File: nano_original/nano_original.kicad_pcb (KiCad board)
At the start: 2 copper layers, 43.2 x 18 mm, 29 parts, among them J1 USB_B_Micro, J2 Conn_01x15, J3 Conn_01x15, J4 Conn_02x03_Odd_Even, SW1 SW_Push, U1 LM1117MP-5.0, U2 FT231XS, U3 ATmega328P-MUR, Y1 16MHz

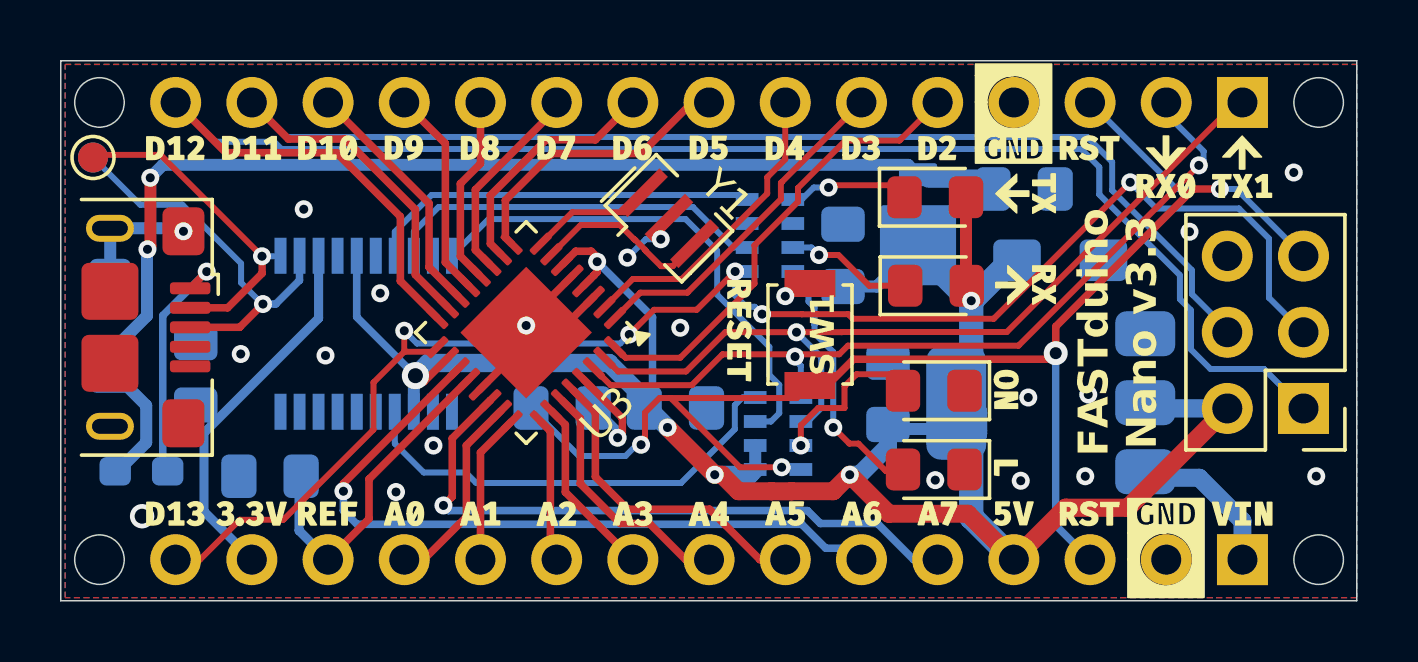
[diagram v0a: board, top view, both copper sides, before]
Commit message: critical fix: swap tx and rx between atmega328p and ft231 (smooth brain moment)
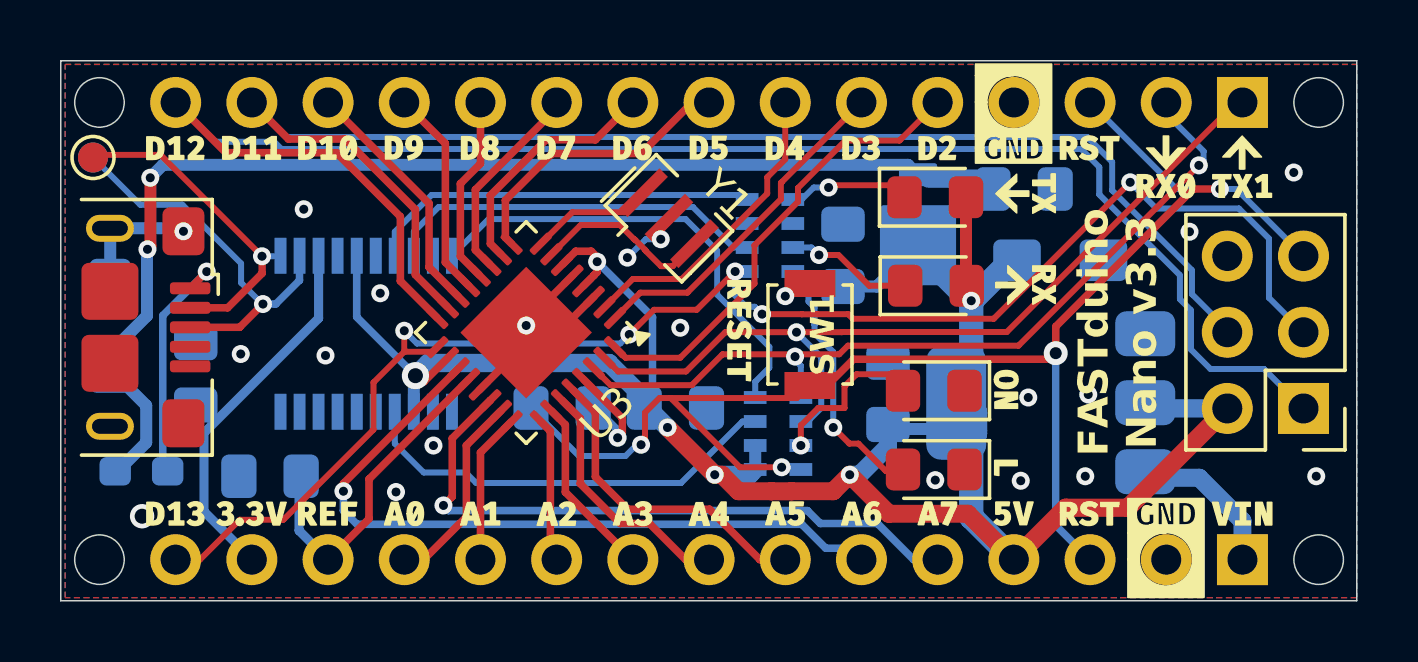
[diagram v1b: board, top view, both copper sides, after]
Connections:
- U2 pad 20: /TX -> /RX
- U2 pad 4: /RX -> /TX
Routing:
- net /TX: track 17.0 -> 14.5 mm
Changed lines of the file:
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@@
 			(size 1.2 0.4)
 			(layers "B.Cu" "B.Mask" "B.Paste")
-			(net 3 "/RX")
+			(net 6 "/TX")
 			(pinfunction "RXD")
 			(pintype "input")
@@
 			(size 1.2 0.4)
 			(layers "B.Cu" "B.Mask" "B.Paste")
-			(net 6 "/TX")
+			(net 3 "/RX")
 			(pinfunction "TXD")
 			(pintype "output")
@@
 	)
 	(segment
-		(start 79.825 88.075)
-		(end 73 88.075)
+		(start 81.02918 81.79628)
+		(end 81.02918 80.32918)
 		(width 0.2)
 		(layer "B.Cu")
@@
 	)
 	(segment
-		(start 72.65 87.725)
-		(end 71.25 87.725)
+		(start 82.770254 84.229746)
+		(end 82.770254 83.537354)
 		(width 0.2)
 		(layer "B.Cu")
@@
 	)
 	(segment
-		(start 81.619 86.281)
-		(end 79.825 88.075)
+		(start 73.413 79.277)
+		(end 72.19 80.5)
 		(width 0.2)
 		(layer "B.Cu")
@@
 	)
 	(segment
-		(start 81.619 85.481)
-		(end 81.619 86.281)
+		(start 82.3 84.7)
+		(end 82.770254 84.229746)
 		(width 0.2)
 		(layer "B.Cu")
@@
 	)
 	(segment
-		(start 81.875 85.225)
-		(end 81.619 85.481)
+		(start 79.977 79.277)
+		(end 73.413 79.277)
 		(width 0.2)
 		(layer "B.Cu")
@@
 	)
 	(segment
-		(start 73 88.075)
-		(end 72.65 87.725)
+		(start 82.770254 83.537354)
+		(end 81.02918 81.79628)
 		(width 0.2)
 		(layer "B.Cu")
@@
 	)
 	(segment
-		(start 70.285 86.76)
-		(end 70.285 85.7)
+		(start 82.3 85.225)
+		(end 82.3 84.7)
 		(width 0.2)
 		(layer "B.Cu")
@@
 	)
 	(segment
-		(start 82.3 85.225)
-		(end 81.875 85.225)
-		(width 0.2)
-		(layer "B.Cu")
-		(net 3)
-	)
-	(segment
-		(start 71.25 87.725)
-		(end 70.285 86.76)
+		(start 81.02918 80.32918)
+		(end 79.977 79.277)
 		(width 0.2)
 		(layer "B.Cu")
@@
 	)
 	(segment
-		(start 81.02918 80.32918)
-		(end 79.977 79.277)
+		(start 70.285 86.76)
+		(end 70.285 85.7)
 		(width 0.2)
 		(layer "B.Cu")
@@
 	)
 	(segment
-		(start 81.02918 81.79628)
-		(end 81.02918 80.32918)
+		(start 71.25 87.725)
+		(end 70.285 86.76)
 		(width 0.2)
 		(layer "B.Cu")
@@
 	)
 	(segment
-		(start 82.770254 84.470254)
-		(end 82.770254 83.537354)
+		(start 81.875 86.025)
+		(end 79.825 88.075)
 		(width 0.2)
 		(layer "B.Cu")
@@
 	)
 	(segment
-		(start 82.825 86.025)
-		(end 83.1 85.75)
+		(start 82.3 86.025)
+		(end 81.875 86.025)
 		(width 0.2)
 		(layer "B.Cu")
@@
 	)
 	(segment
-		(start 79.977 79.277)
-		(end 73.413 79.277)
+		(start 79.825 88.075)
+		(end 73 88.075)
 		(width 0.2)
 		(layer "B.Cu")
@@
 	)
 	(segment
-		(start 83.1 85.75)
-		(end 83.1 84.8)
+		(start 73 88.075)
+		(end 72.65 87.725)
 		(width 0.2)
 		(layer "B.Cu")
@@
 	)
 	(segment
-		(start 82.770254 83.537354)
-		(end 81.02918 81.79628)
-		(width 0.2)
-		(layer "B.Cu")
-		(net 6)
-	)
-	(segment
-		(start 83.1 84.8)
-		(end 82.770254 84.470254)
-		(width 0.2)
-		(layer "B.Cu")
-		(net 6)
-	)
-	(segment
-		(start 82.3 86.025)
-		(end 82.825 86.025)
-		(width 0.2)
-		(layer "B.Cu")
-		(net 6)
-	)
-	(segment
-		(start 73.413 79.277)
-		(end 72.19 80.5)
-		(width 0.2)
-		(layer "B.Cu")
+		(start 72.65 87.725)
+		(end 71.25 87.725)
+		(width 0.2)
+		(layer "B.Cu")
